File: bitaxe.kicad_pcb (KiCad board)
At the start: 4 copper layers, 59.5 x 61.2 mm, 94 parts, among them IC1 BM1387, IC2 BM1387, IC3 MIC5317, IC4 MIC5317, J2 Conn_01x02, J3 Conn_01x05, J4 Conn_01x02, J5 Conn_01x03, Y1 25MHz

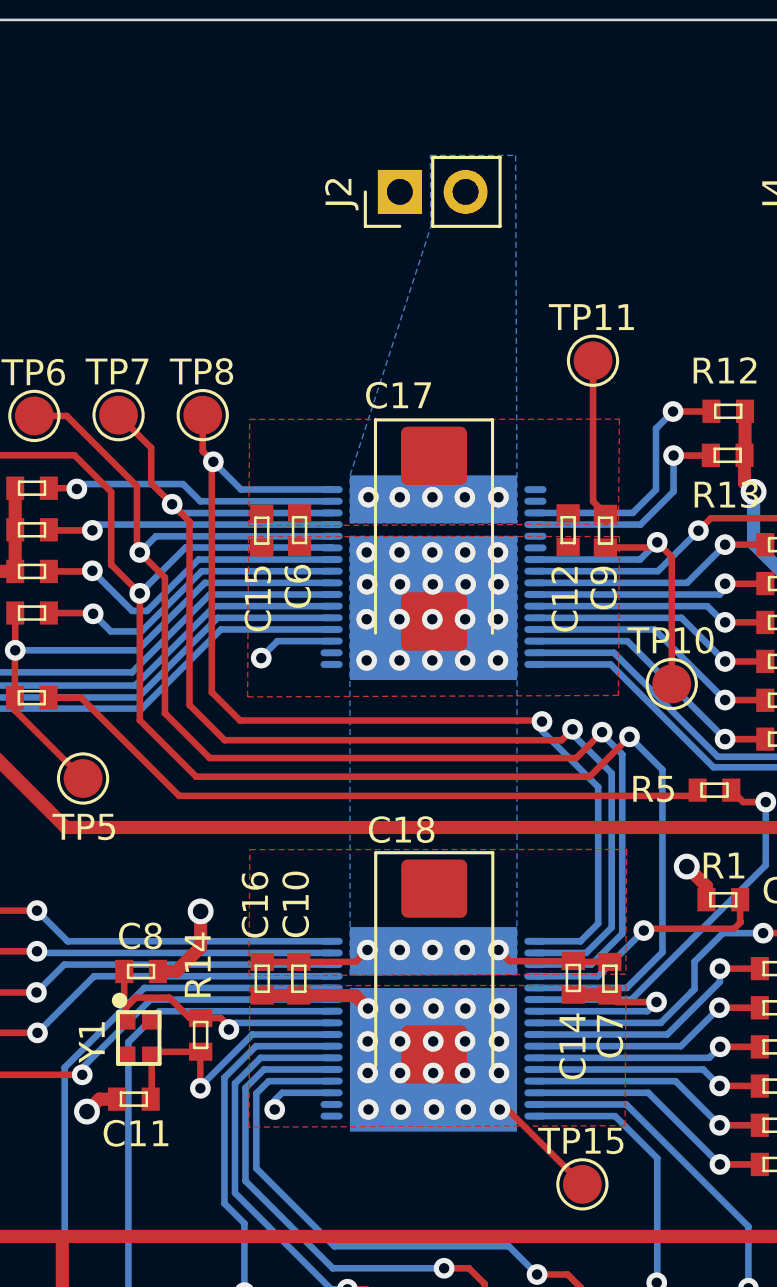
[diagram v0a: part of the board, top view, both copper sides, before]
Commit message: shrink the power pads for #4 and switched the BM1387 pin pitch to 0.48mm for #5. still need to fix PCB
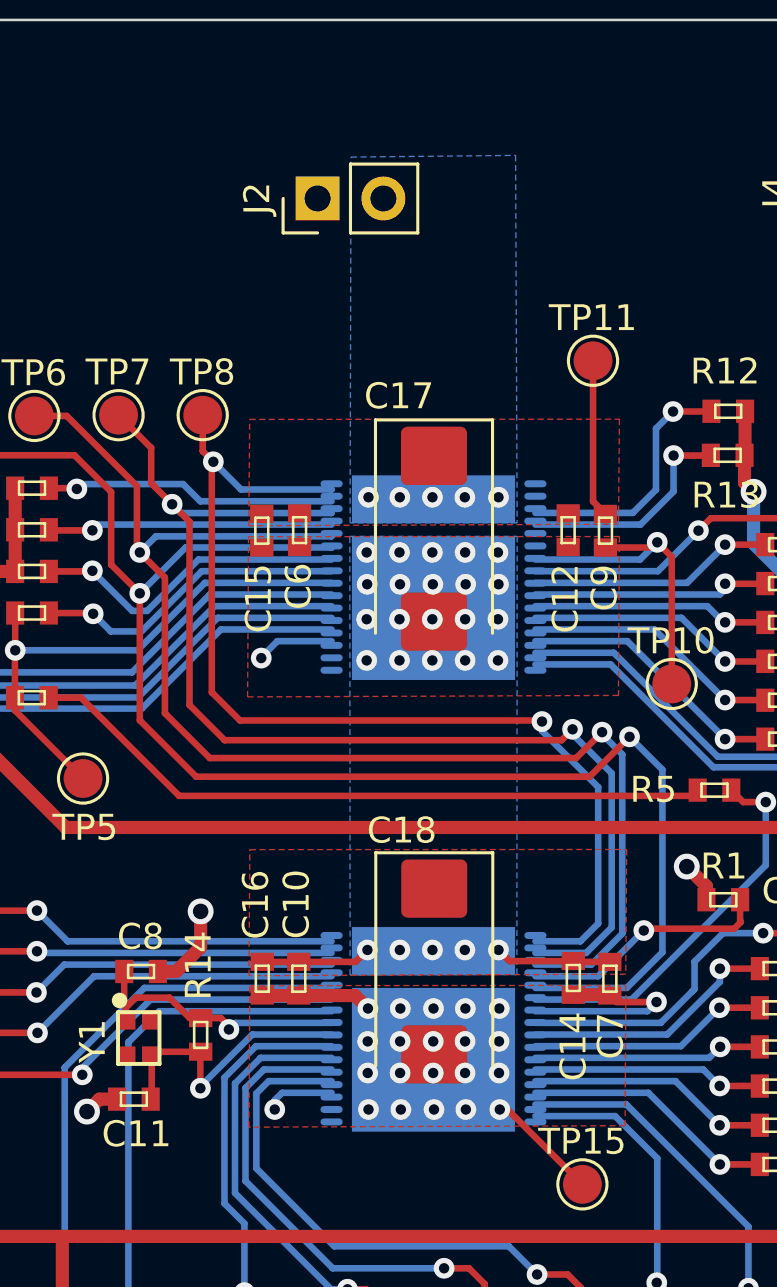
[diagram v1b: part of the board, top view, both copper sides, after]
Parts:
- moved J2 3.19 mm to (84.8, 53.0)
